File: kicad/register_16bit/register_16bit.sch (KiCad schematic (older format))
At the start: 38 parts, among them J1 DB37_Male, U1 SN74ALVC00

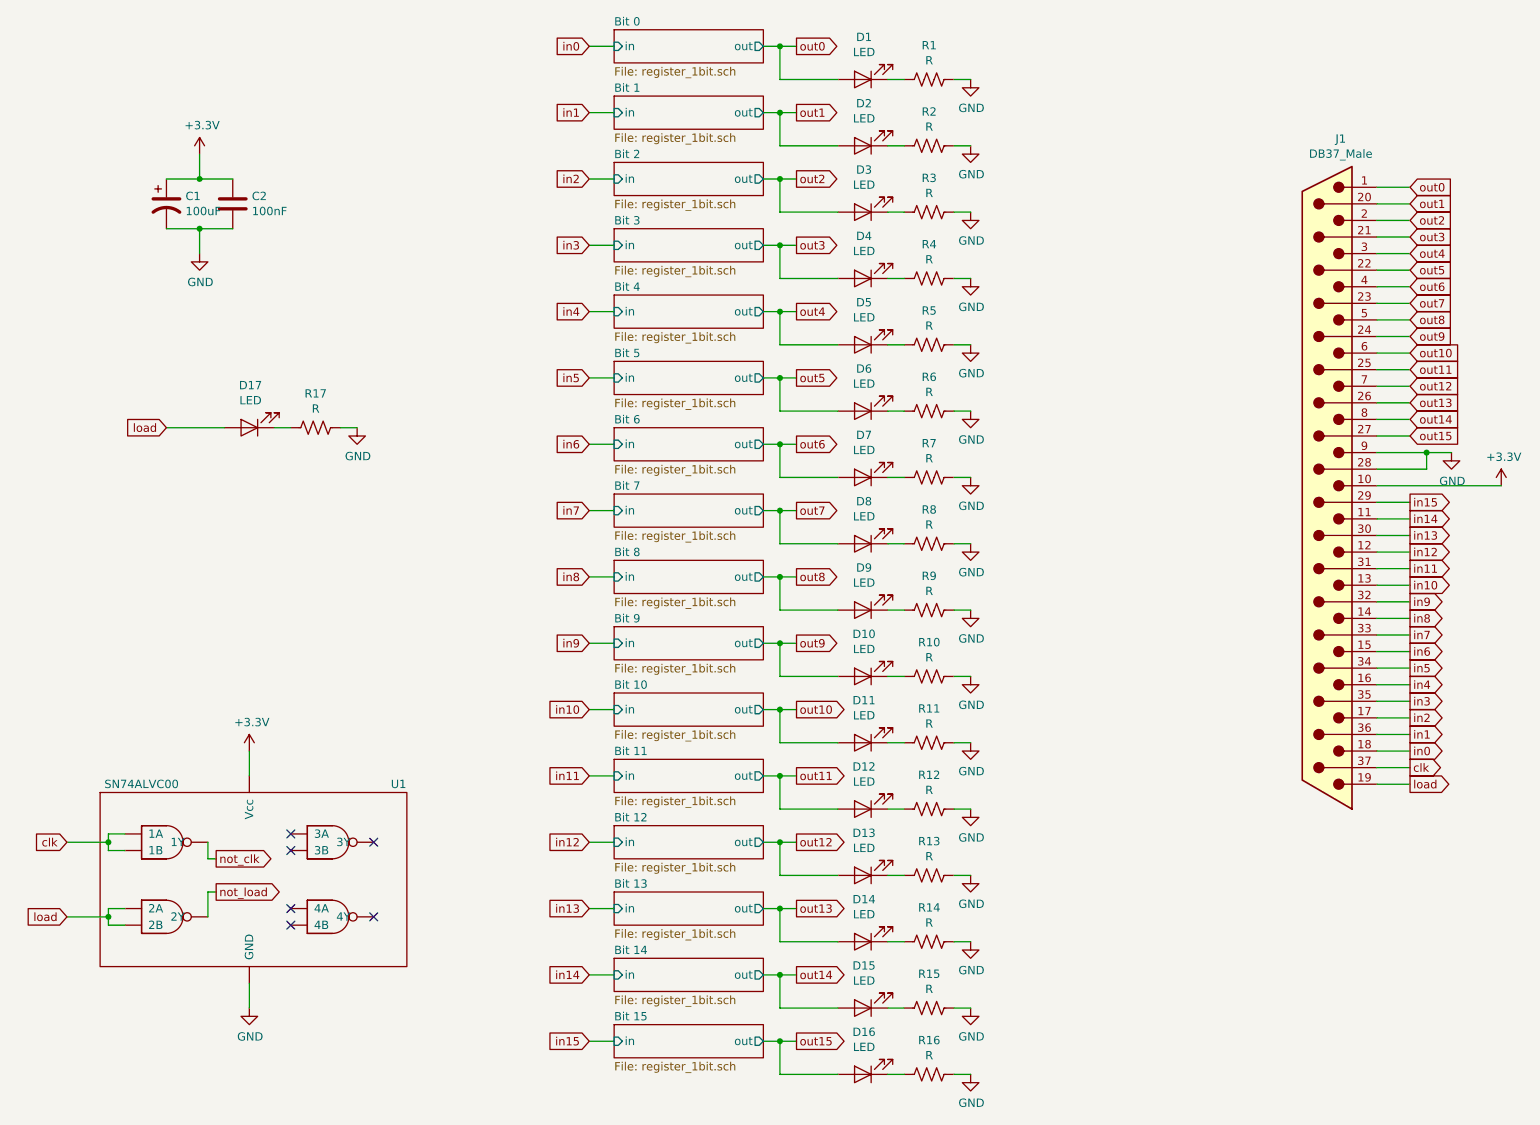
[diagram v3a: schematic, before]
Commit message: Readme updates (#6)
* Readme intro section

* Board revisions for manufacturing, add digikey PNs to all, added logo.
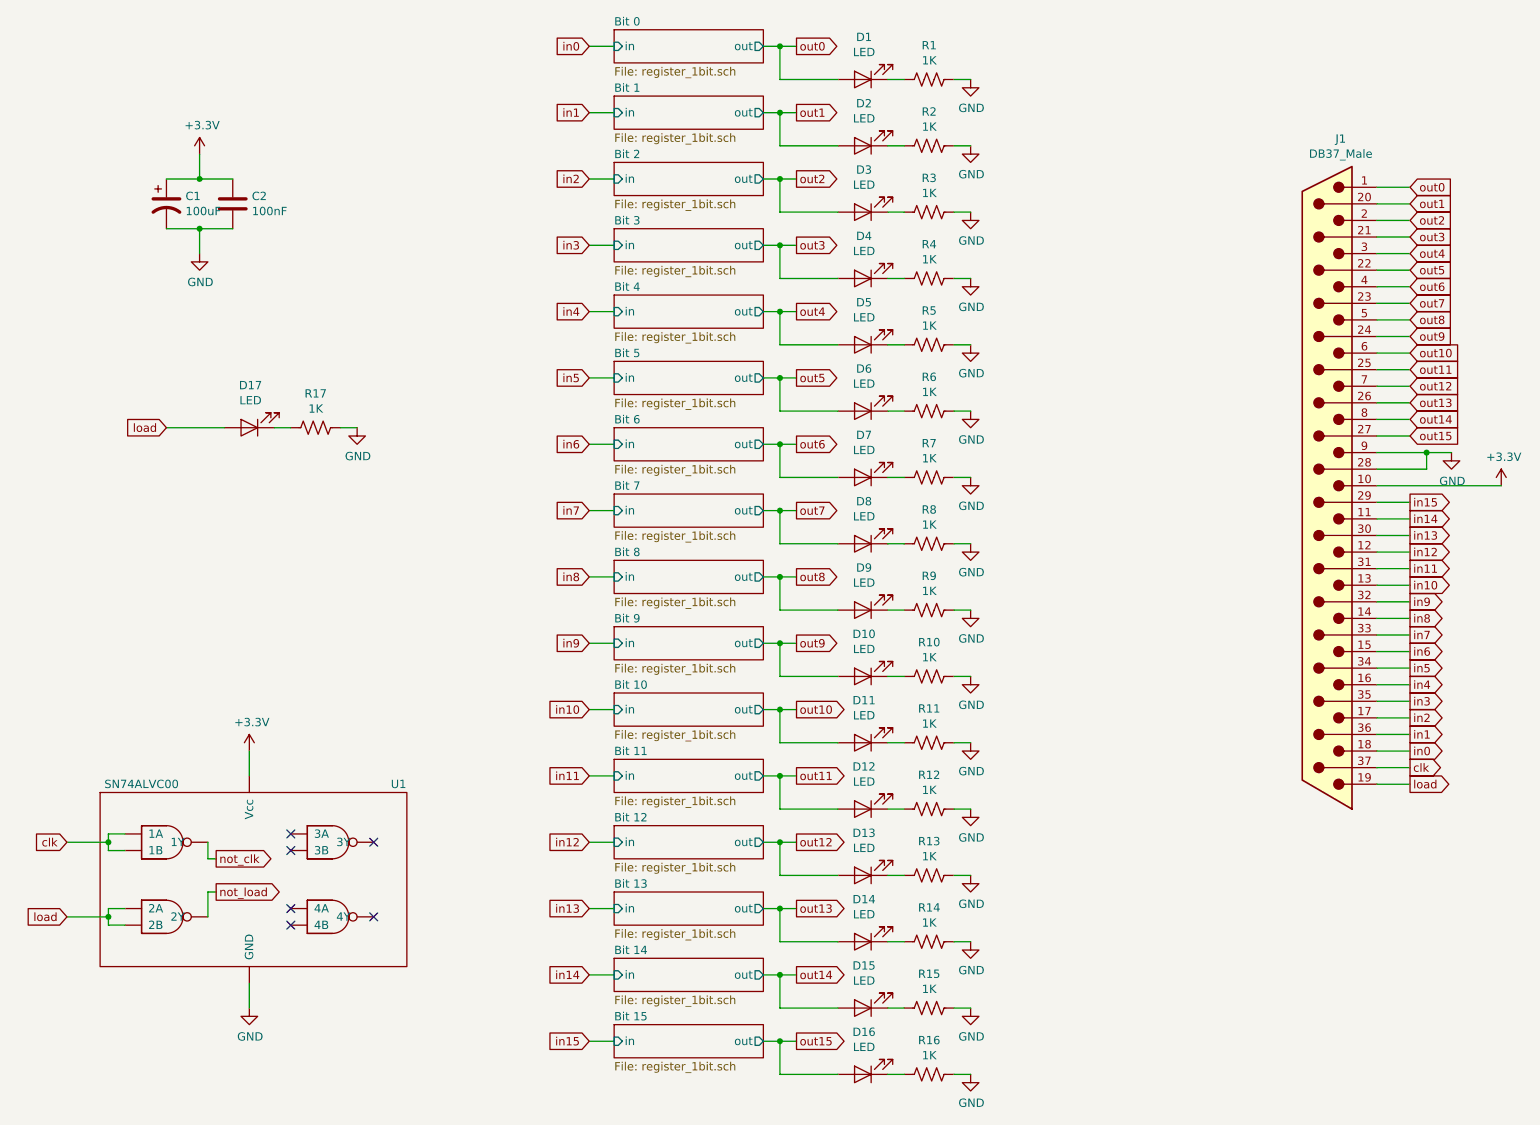
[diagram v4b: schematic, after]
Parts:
- J1: footprint Connector_Dsub:DSUB-37_Male_Horizontal_P2.77x2.84mm_EdgePinOffset4.94mm_Housed_MountingHolesOffset7.48mm -> Connector_Dsub:DSUB-37_Male_Horizontal_P2.77x2.84mm_EdgePinOffset7.70mm_Housed_MountingHolesOffset9.12mm; Digikey PN (none) -> AE10986-ND
- R1, R10, R11, R12, R13, R14, R15, R16, R17, R2, R3, R4, R5, R6, R7, R8, R9: value R -> 1K; Digikey PN (none) -> P1.0KECT-ND
- U1: Digikey PN (none) -> 296-5104-1-ND
